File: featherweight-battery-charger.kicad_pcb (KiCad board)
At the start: 2 copper layers, 20.3 x 32.7 mm, 13 parts, among them J2 Conn_01x02, J3 Conn_01x02, J4 Conn_01x02, U1 MCP73832-2-OT

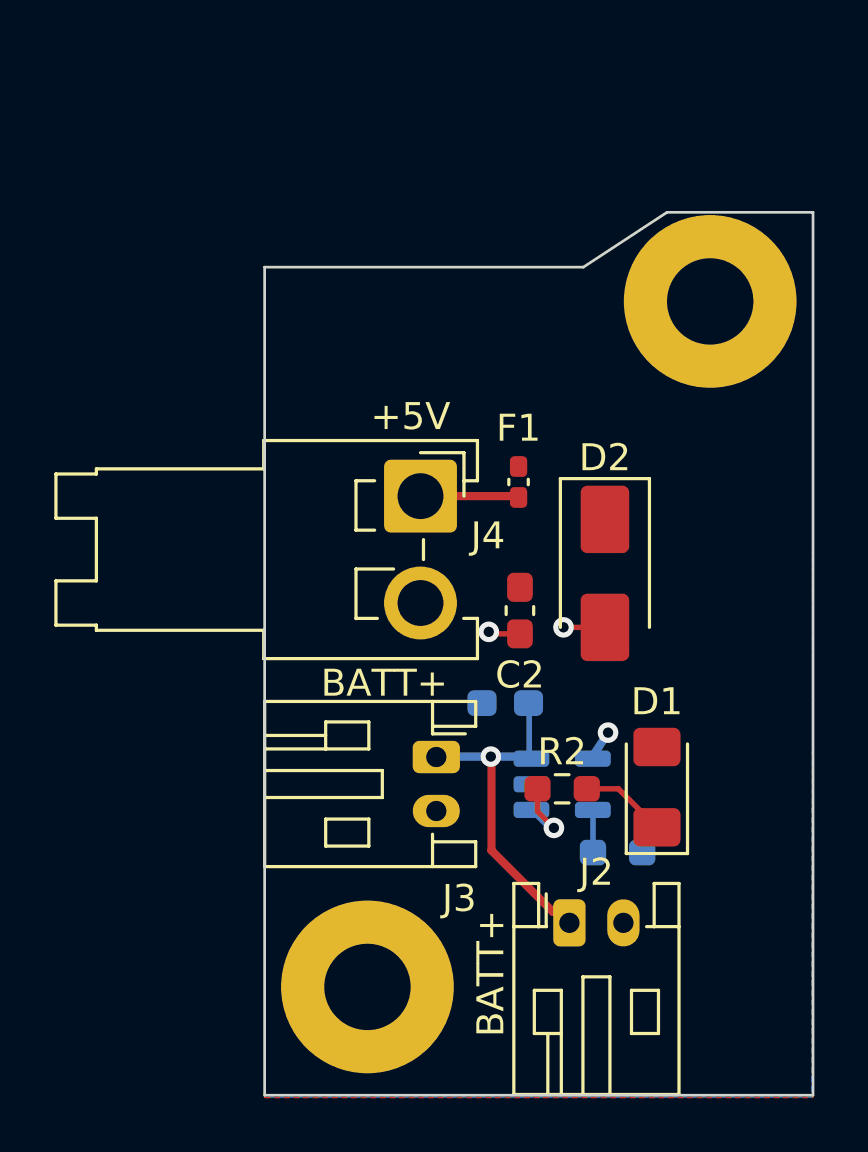
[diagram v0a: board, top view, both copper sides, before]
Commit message: Changed Layout and Routing, Added Calculation Comments and Batt plane for  heat diff. Fuse changed to 1206
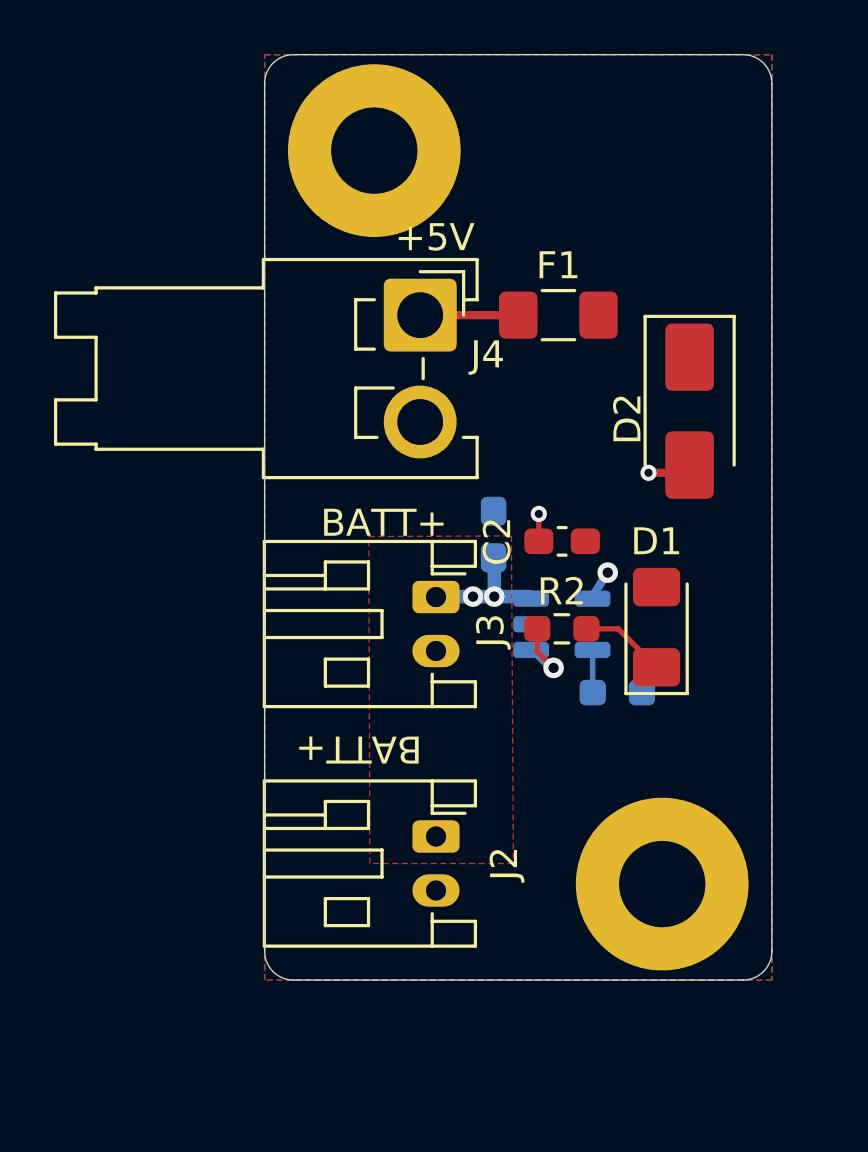
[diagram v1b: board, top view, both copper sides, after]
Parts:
- D1: value LED -> RLED
- F1: value ERB-RD0R50X (500mA) -> 0ZCJ0050FF2G (500mA); footprint Fuse:Fuse_0402_1005Metric_Pad0.77x0.64mm_HandSolder -> Fuse:Fuse_1206_3216Metric_Pad1.42x1.75mm_HandSolder
- R2: value 133 -> 200
- moved H1 13.6 mm to (147.8, 71.6)
- moved H2 11.6 mm to (158.5, 98.8)
- moved D2 6.78 mm to (159.5, 81.3)
- moved J4 6.71 mm to (149.5, 77.7)
- moved F1 6.36 mm to (154.6, 77.7), turned to 0 degrees
- moved C3 6.26 mm to (152.2, 85.9), turned to 90 degrees
- moved R1 5.93 mm to (156.8, 91.7)
- moved D1 5.93 mm to (158.3, 89.3)
- moved J3 5.93 mm to (150.1, 88.2)
- moved R2 5.93 mm to (154.8, 89.3)
- moved U1 5.93 mm to (154.8, 89.2)
- moved J2 5.89 mm to (150.1, 97.0), turned to -90 degrees
- moved C2 3.00 mm to (154.8, 86.1), turned to 180 degrees
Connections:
- net Net-(J2-Pin_1) renamed +BATT
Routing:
- net +BATT: track 12.5 -> 4.98 mm, vias 1 -> 2
- added copper zone on F.Cu, net +BATT
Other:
- board size 20.3 x 32.7 mm -> 18.8 x 34.3 mm
